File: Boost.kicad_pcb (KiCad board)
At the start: 2 copper layers, 83.3 x 47.7 mm, 28 parts, among them Q1 2N2222, Q2 2N2907, U1 SG3525, U2 LM7808_TO220

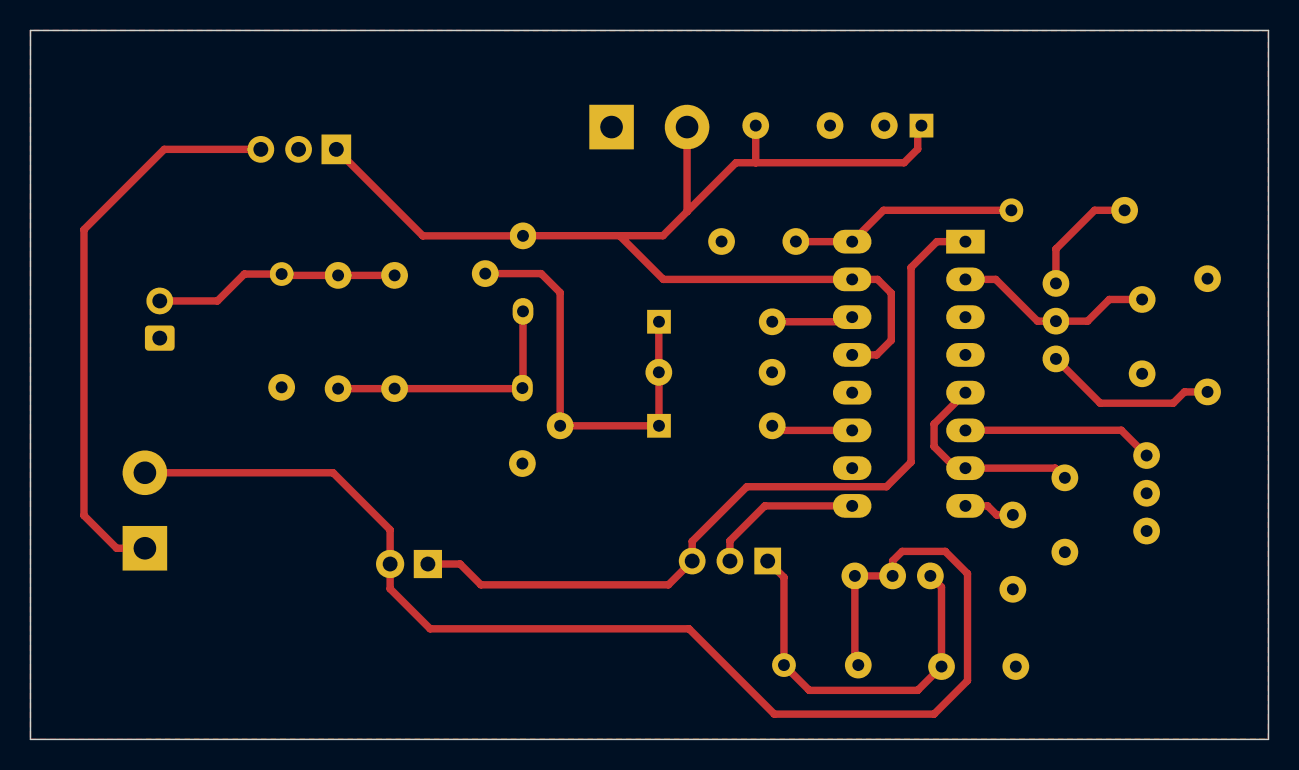
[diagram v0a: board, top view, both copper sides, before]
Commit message: Remoção das zonas de cobre
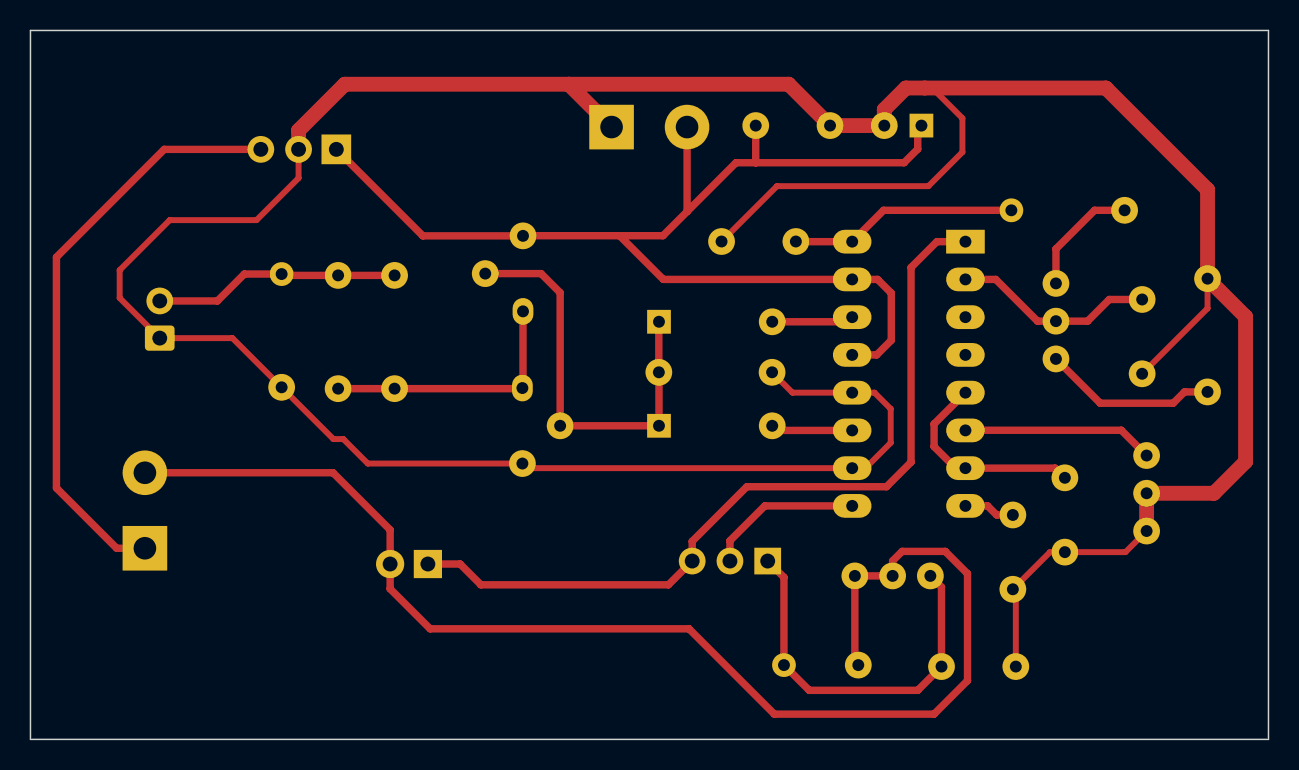
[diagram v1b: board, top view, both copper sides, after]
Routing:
- net GNDREF: track 0.00 -> 238.4 mm
- net Net-(J3-Pin_1): track 38.4 -> 39.9 mm
- removed copper zone on F.Cu, net GNDREF
